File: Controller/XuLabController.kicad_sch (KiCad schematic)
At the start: 24 parts, among them J10 Servo, J11 Servo, J12 Thruster, J14 I2C, J15 I2C, J16 UART1, J17 UART2, J18 SPI1, J19 SPI2, J20 Interrupt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

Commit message: Remove power schematic from controller board
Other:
- removed sheet Power
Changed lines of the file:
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@@
-	)
-	(sheet
-		(at 50.8 152.4)
-		(size 38.1 25.4)
-		(exclude_from_sim no)
-		(in_bom yes)
-		(on_board yes)
-		(dnp no)
-		(fields_autoplaced yes)
-		(stroke
-			(width 0.1524)
-			(type solid)
-		)
-		(fill
-			(color 0 0 0 0.0000)
-		)
-		(property "Sheetname" "Power"
-			(at 50.8 151.6884 0)
-			(effects
-				(font
-					(size 1.27 1.27)
-				)
-				(justify left bottom)
-			)
-		)
-		(property "Sheetfile" "Power.kicad_sch"
-			(at 50.8 178.3846 0)
-			(effects
-				(font
-					(size 1.27 1.27)
-				)
-				(justify left top)
-			)
-		)
-		(instances
-			(project "XuLabPlatform"
-				(path "/71bb14ae-b730-4d22-a41d-cf68989dae2d"
-					(page "4")
-				)
-			)
-		)
 	)
 	(sheet
@@
 		)
 		(instances
-			(project "XuLabPlatform"
+			(project "XuLabController"
 				(path "/71bb14ae-b730-4d22-a41d-cf68989dae2d"
 					(page "2")
@@
 		)
 		(instances
-			(project "XuLabPlatform"
+			(project "XuLabController"
 				(path "/71bb14ae-b730-4d22-a41d-cf68989dae2d"
 					(page "3")

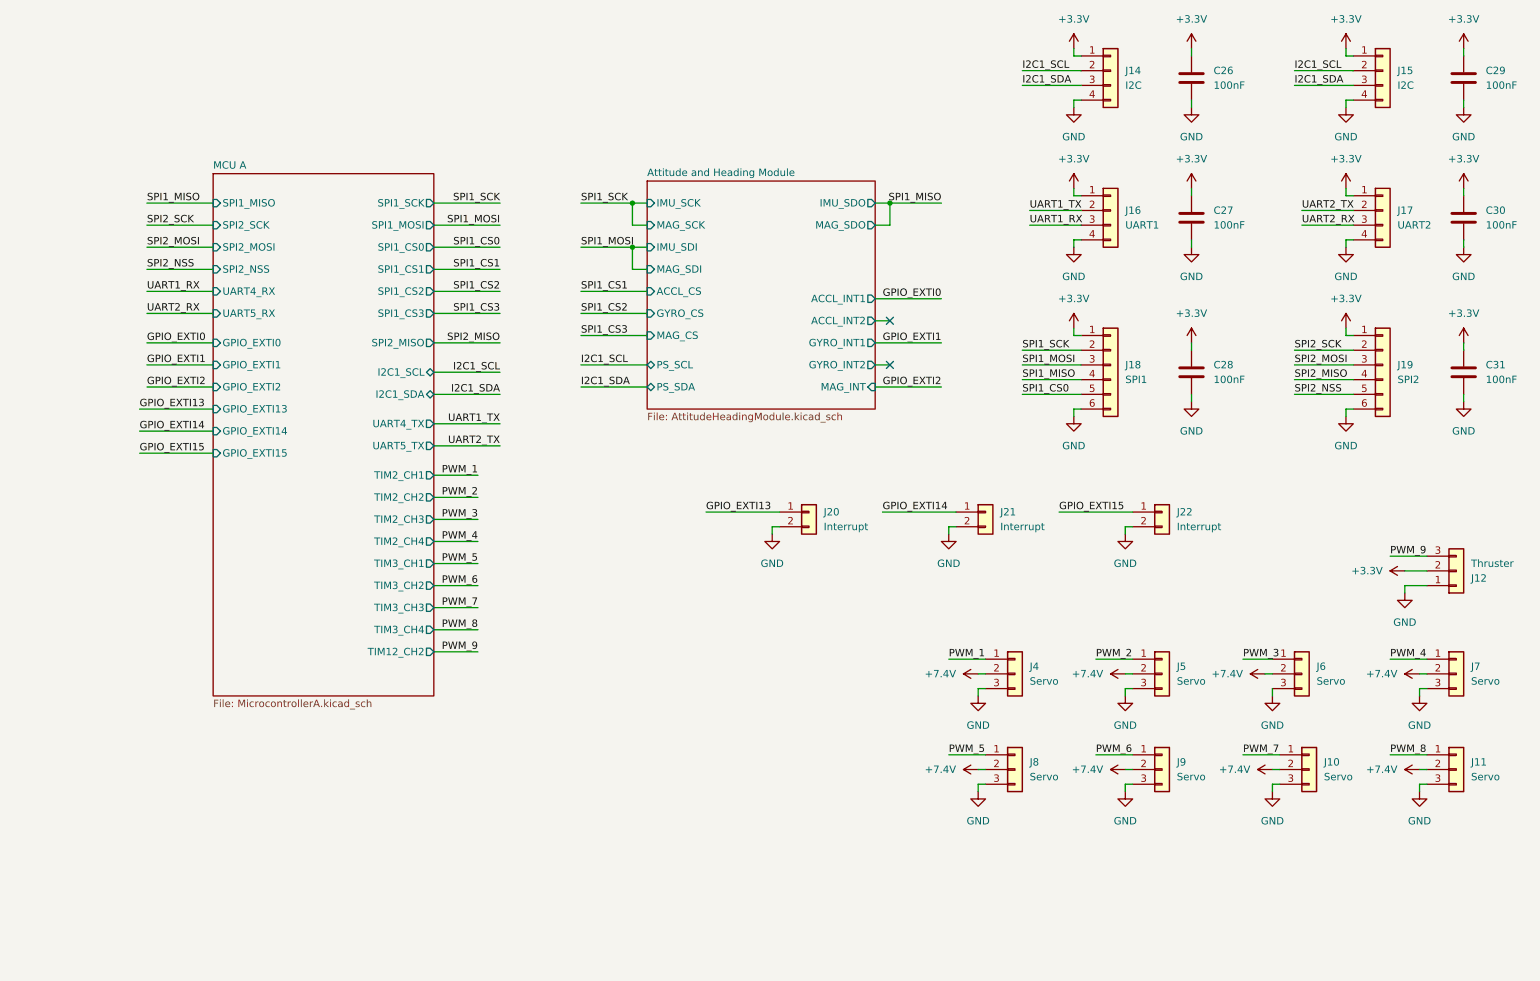
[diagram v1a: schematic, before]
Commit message: Reorganize controller schematic
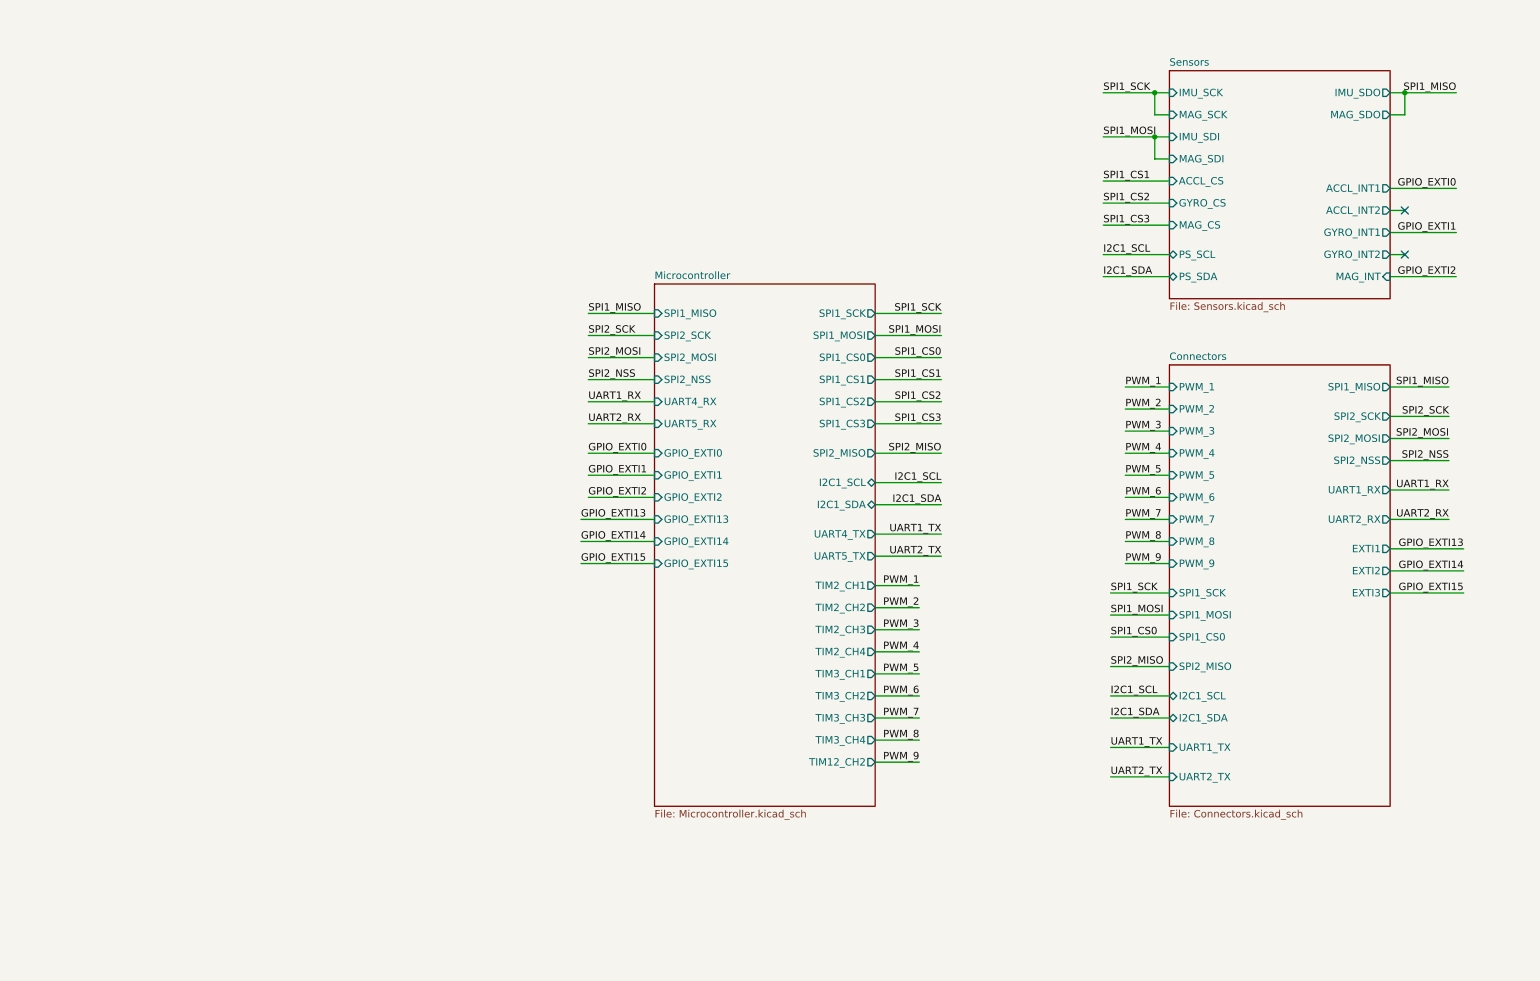
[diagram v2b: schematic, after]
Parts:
- removed C26, C27, C28, C29, C30, C31: 100nF, Capacitor_SMD:C_0402_1005Metric, symbol Device:C
- removed J10, J11, J4, J5, J6, J7, J8, J9: Servo, Connector_JST:JST_VH_B3P-VH-B_1x03_P3.96mm_Vertical, symbol Connector_Generic:Conn_01x03
- removed J12: Thruster, Connector_JST:JST_VH_B3P-VH-B_1x03_P3.96mm_Vertical, symbol Connector_Generic:Conn_01x03
- removed J14, J15: I2C, Connector_Molex:Molex_PicoBlade_53048-0410_1x04_P1.25mm_Horizontal, symbol Connector_Generic:Conn_01x04
- removed J16: UART1, Connector_Molex:Molex_PicoBlade_53048-0410_1x04_P1.25mm_Horizontal, symbol Connector_Generic:Conn_01x04
- removed J17: UART2, Connector_Molex:Molex_PicoBlade_53048-0410_1x04_P1.25mm_Horizontal, symbol Connector_Generic:Conn_01x04
- removed J18: SPI1, Connector_Molex:Molex_PicoBlade_53048-0610_1x06_P1.25mm_Horizontal, symbol Connector_Generic:Conn_01x06
- removed J19: SPI2, Connector_Molex:Molex_PicoBlade_53048-0610_1x06_P1.25mm_Horizontal, symbol Connector_Generic:Conn_01x06
- removed J20, J21, J22: Interrupt, Connector_Molex:Molex_KK-254_AE-6410-02A_1x02_P2.54mm_Vertical, symbol Connector_Generic:Conn_01x02
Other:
- sheet Attitude and Heading Module renamed Sensors
- sheet MCU A renamed Microcontroller
- added sheet Connectors (Connectors.kicad_sch)
- sheet Microcontroller: file MicrocontrollerA.kicad_sch -> Microcontroller.kicad_sch
- sheet Sensors: file AttitudeHeadingModule.kicad_sch -> Sensors.kicad_sch

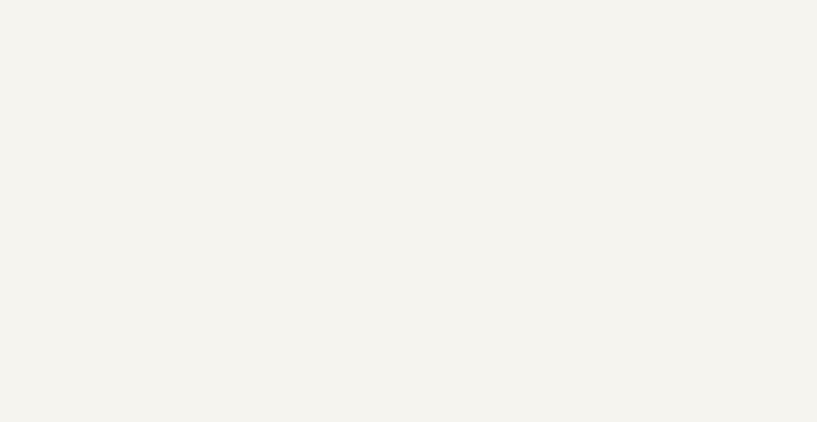
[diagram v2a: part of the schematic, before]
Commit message: Add power input connector to controller schematic
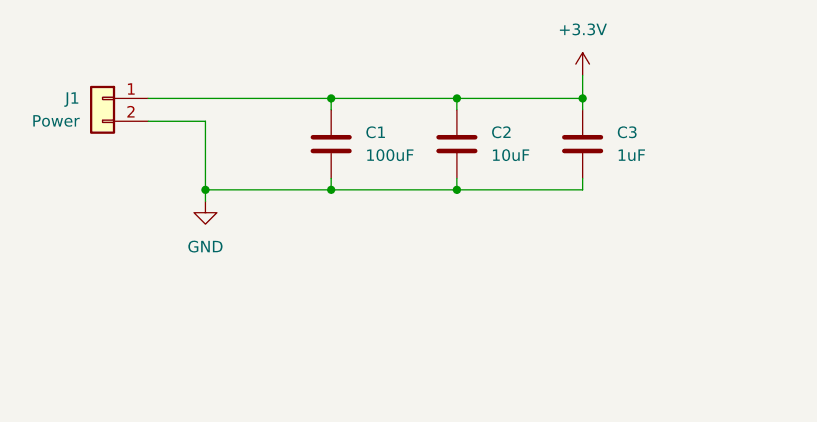
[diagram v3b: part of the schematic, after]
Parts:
- added C1: 100uF, Capacitor_SMD:C_1210_3225Metric, symbol Device:C
- added C2: 10uF, Capacitor_SMD:C_1206_3216Metric, symbol Device:C
- added C3: 1uF, Capacitor_SMD:C_0603_1608Metric, symbol Device:C
- added J1: Power, Connector_JST:JST_XH_S2B-XH-A_1x02_P2.50mm_Horizontal, symbol Connector_Generic:Conn_01x02
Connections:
- new net +3.3V: C1.1, C2.1, C3.1, J1.1 (Pin_1)
- new net GND: C1.2, C2.2, C3.2, J1.2 (Pin_2)
